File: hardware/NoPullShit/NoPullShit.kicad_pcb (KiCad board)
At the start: 2 copper layers, 52 parts, among them J1 USB Power, J2 Load cell, J3 Batt+, J4 Batt-, J5 ICSP, J6 UART, J7 Spk+, J8 Spk-, Q1 BC808, Q1 S8550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

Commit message: Initial routing backup
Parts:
- removed the Q1 at (72.5, 67.1)
- removed the Q1 at (33.5, 66.5)
- removed the Q2 at (82.2, 52.4)
- removed the Q2 at (37.9, 66.5)
- removed the Q3 at (80.9, 58.2)
- removed the Q3 at (42.4, 66.5)
- added H1: MountingHole_Pad, MountingHole:MountingHole_2.2mm_M2_Pad_Via, F.Cu at (28.4, 62.4)
- added H2: MountingHole_Pad, MountingHole:MountingHole_2.2mm_M2_Pad_Via, F.Cu at (62.4, 62.4)
- added H3: MountingHole_Pad, MountingHole:MountingHole_2.2mm_M2_Pad_Via, F.Cu at (28.4, 33.4)
- added H4: MountingHole_Pad, MountingHole:MountingHole_2.2mm_M2_Pad_Via, F.Cu at (62.4, 33.4)
- added Q1: BC808, Package_TO_SOT_SMD:SOT-23, F.Cu at (50.8, 55.0)
- added Q2: BC817, Package_TO_SOT_SMD:SOT-23, F.Cu at (55.6, 37.5)
- added Q3: BC808, Package_TO_SOT_SMD:SOT-23, F.Cu at (59.6, 37.5)
- C13, C14: footprint Capacitor_SMD:C_0603_1608Metric -> Capacitor_SMD:C_1206_3216Metric
- J2: footprint Connector_PinHeader_2.54mm:PinHeader_1x04_P2.54mm_Vertical -> Connector_PinHeader_2.00mm:PinHeader_1x04_P2.00mm_Vertical
- J3, J4, J7, J8: footprint Connector_PinHeader_1.00mm:PinHeader_1x01_P1.00mm_Vertical -> TestPoint:TestPoint_THTPad_1.0x1.0mm_Drill0.5mm
- moved R14 71.2 mm to (30.4, 38.4), turned to 180 degrees
- moved C8 58.8 mm to (40.2, 49.5), turned to 270 degrees
- moved R15 53.7 mm to (35.4, 41.3)
- moved C7 52.0 mm to (42.7, 48.9)
- moved C9 51.7 mm to (42.7, 36.2)
- moved C11 51.2 mm to (37.0, 35.5), turned to 90 degrees
- moved R17 51.1 mm to (45.9, 48.9)
- moved R13 48.1 mm to (38.3, 49.5), turned to 270 degrees
- moved R16 47.4 mm to (42.7, 50.8)
- moved R6 44.2 mm to (56.9, 56.7)
- moved C10 43.9 mm to (48.4, 35.5), turned to 90 degrees
- moved D1 41.9 mm to (26.2, 40.6), turned to 270 degrees
- moved R8 41.7 mm to (53.1, 47.2), turned to 90 degrees
- moved R7 41.2 mm to (55.7, 54.8)
- moved J8 40.4 mm to (63.4, 37.6)
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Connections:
- U3 pad 10: /N_BATT_CHRG -> /LED_A
- U3 pad 11: /N_BATT_STDBY -> Net-(U3-Pad11)
- U3 pad 2: /LED_A -> Net-(U3-Pad2)
- U3 pad 25: Net-(U3-Pad25) -> /N_BATT_STDBY
- U3 pad 26: Net-(U3-Pad26) -> /N_BATT_CHRG
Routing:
- net VCC: track 0.00 -> 57.1 mm
- net Net-(C3-Pad1): track 0.00 -> 32.2 mm
- net /N_BATT_CHRG: track 0.00 -> 21.5 mm
- net /N_BATT_STDBY: track 0.00 -> 18.8 mm
- net Net-(C8-Pad1): track 0.00 -> 18.4 mm
- net Net-(J5-Pad5): track 0.00 -> 15.9 mm, vias 0 -> 1
- net Net-(C5-Pad2): track 0.00 -> 15.4 mm
- net Net-(C1-Pad1): track 0.00 -> 14.6 mm
- net Net-(J5-Pad3): track 0.00 -> 13.0 mm
- net Net-(J1-Pad1): track 0.00 -> 12.2 mm
- net Net-(C10-Pad2): track 0.00 -> 12.1 mm
- net Net-(C13-Pad2): track 0.00 -> 10.7 mm
- net Net-(J2-Pad2): track 0.00 -> 9.37 mm
- net Net-(J2-Pad3): track 0.00 -> 9.28 mm
- net Net-(Q2-Pad1): track 0.00 -> 8.89 mm
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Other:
- board outline added: 40 x 35 mm
- board text added: "A+"
- board text added: "A-"
- board text added: "Batt+"
- board text added: "Batt-"
- board text added: "E+"
- board text added: "E-"
- board text added: "Sp+"
- board text added: "Sp-"

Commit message: Finished initla routing
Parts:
- moved R18 7.08 mm to (49.8, 35.5)
- moved C12 5.79 mm to (55.1, 39.5)
- moved C10 2.83 mm to (48.5, 32.7)
- moved Q3 2.51 mm to (57.8, 35.7)
- moved Q2 2.51 mm to (53.8, 35.7)
- moved C13 1.61 mm to (59.7, 41.8)
- moved C14 1.61 mm to (59.7, 39.2)
- moved J7 0.57 mm to (63.9, 42.9)
- moved J8 0.57 mm to (63.9, 37.8)
- moved R16 0.47 mm to (42.7, 51.2)
- moved C8 0.30 mm to (39.9, 49.5)
- moved C9 0.25 mm to (42.7, 35.9)
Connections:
- U3 pad 1: /RATE -> /DOUT
- U3 pad 14: /SCK -> Net-(U3-Pad14)
- U3 pad 2: Net-(U3-Pad2) -> /SCK
- U3 pad 32: /DOUT -> /RATE
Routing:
- net GND: track 0.00 -> 28.3 mm, vias 0 -> 24
- net /SCK: track 0.00 -> 23.2 mm
- net /DOUT: track 0.00 -> 20.4 mm
- net Net-(J5-Pad4): track 6.73 -> 23.4 mm, vias 0 -> 2
- net /RATE: track 0.00 -> 12.8 mm
- net /LED_A: track 0.00 -> 12.7 mm
- net /LED_B: track 0.00 -> 7.78 mm
- net Net-(D1-Pad1): track 0.00 -> 4.00 mm
- net VCC: track 57.1 -> 59.4 mm, vias 0 -> 4
- net Net-(J5-Pad5): track 15.9 -> 17.9 mm
- net Net-(Q2-Pad1): track 8.89 -> 7.34 mm
- net Net-(C13-Pad2): track 10.7 -> 11.8 mm
- added copper zone on B.Cu, net GND
- added copper zone on F.Cu, net GND

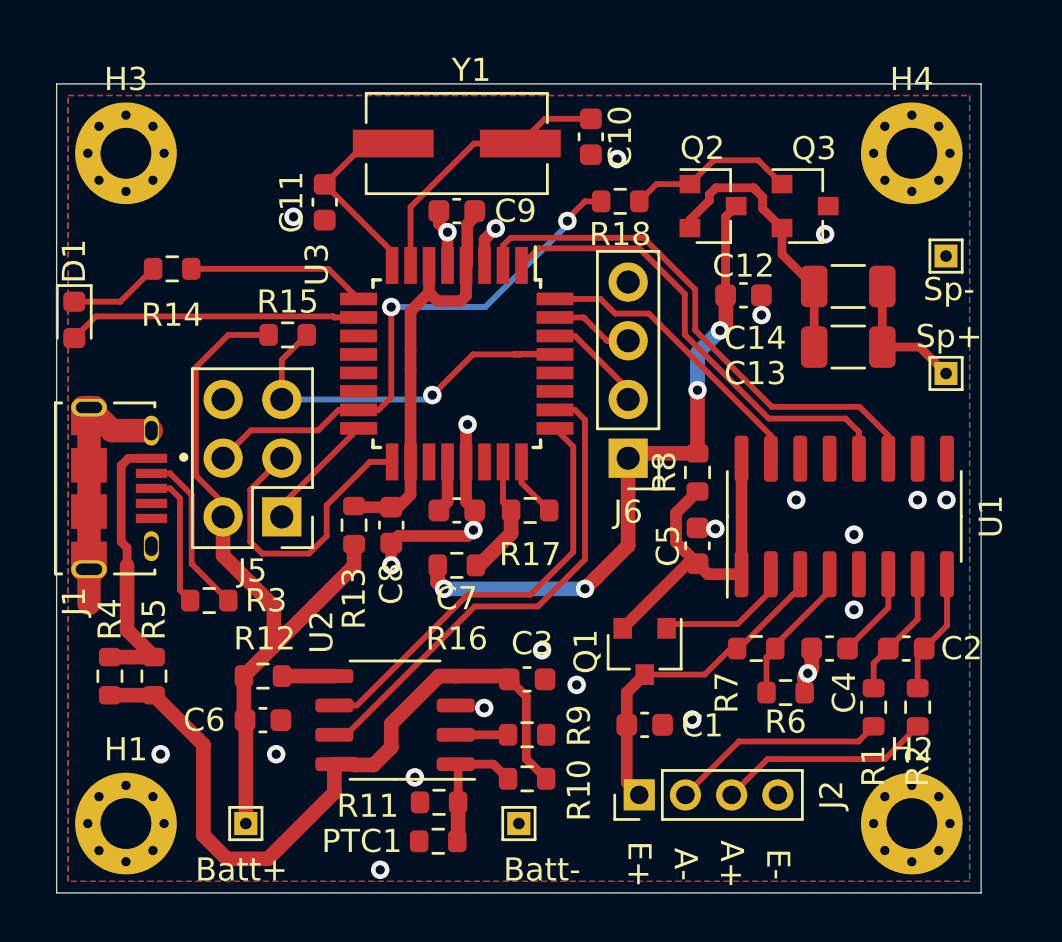
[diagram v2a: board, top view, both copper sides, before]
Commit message: Fixed RefDes placement
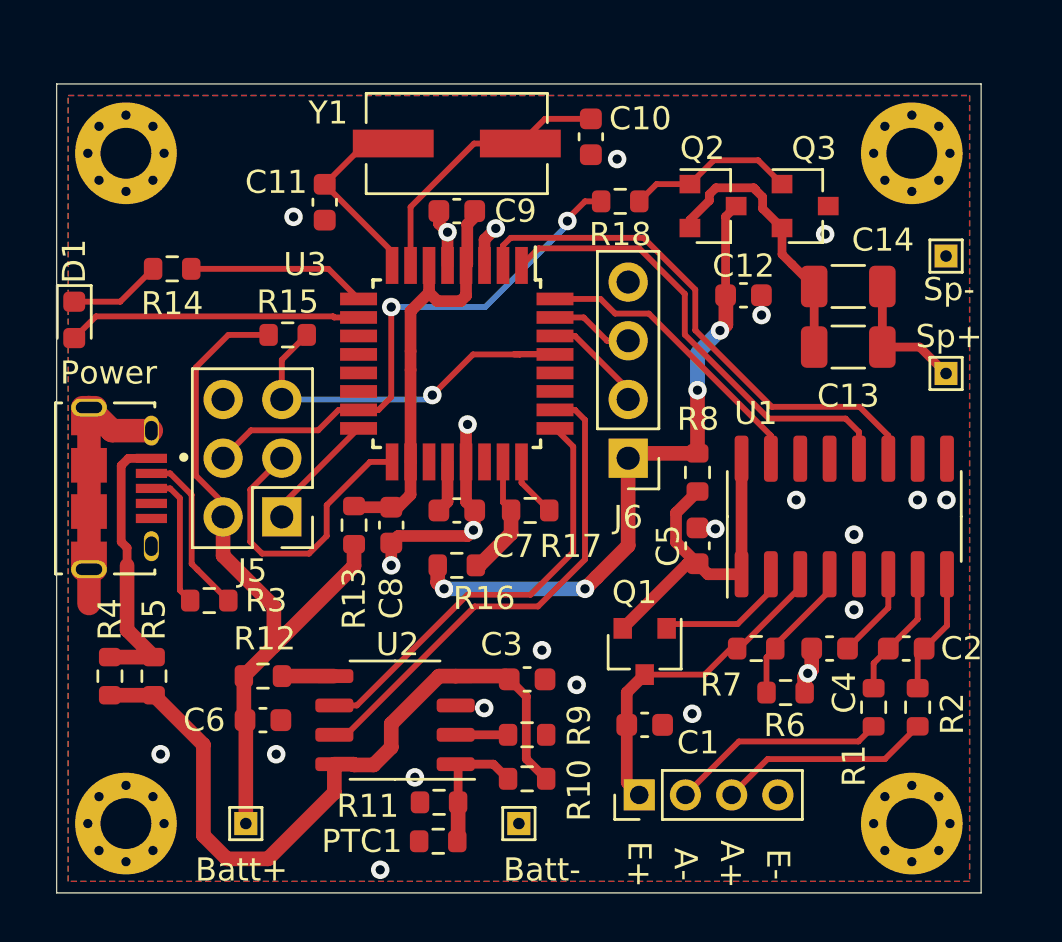
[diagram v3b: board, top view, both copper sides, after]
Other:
- board text added: "Power"

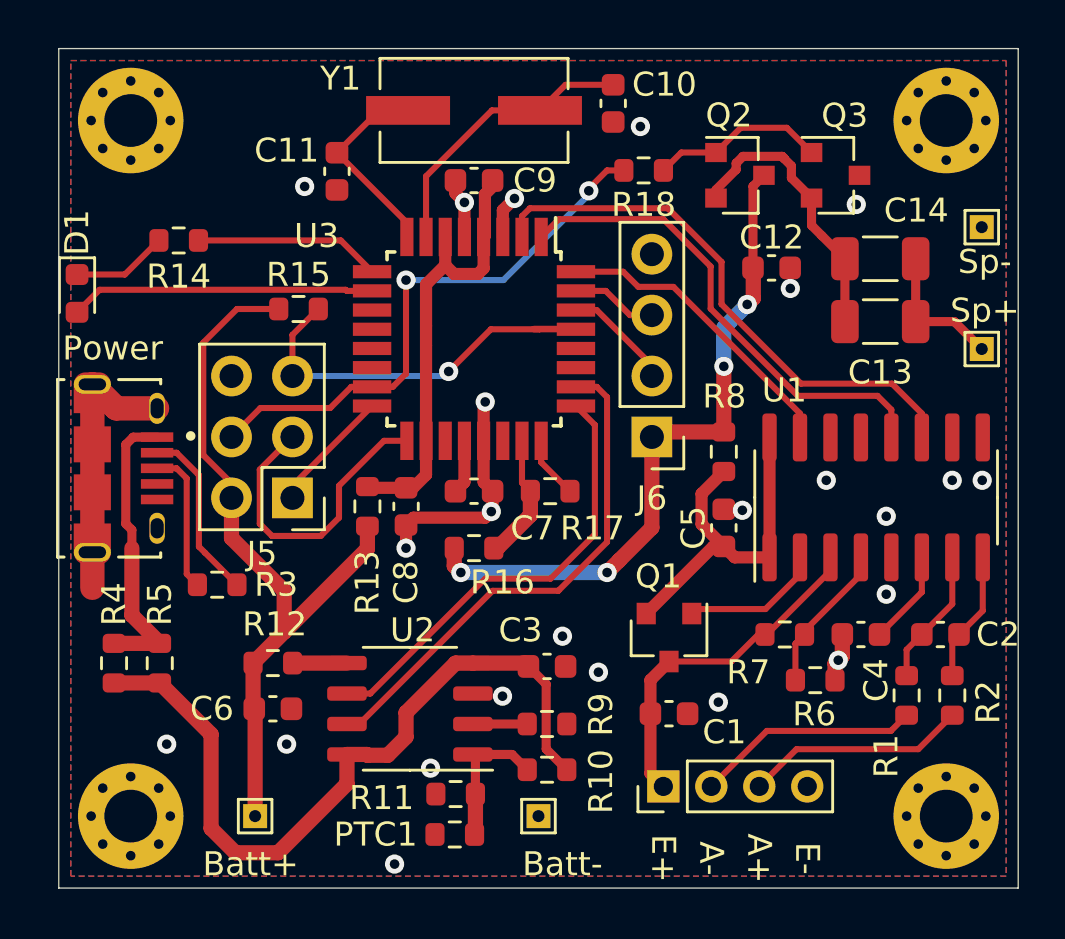
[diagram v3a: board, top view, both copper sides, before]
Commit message: Small layout changes
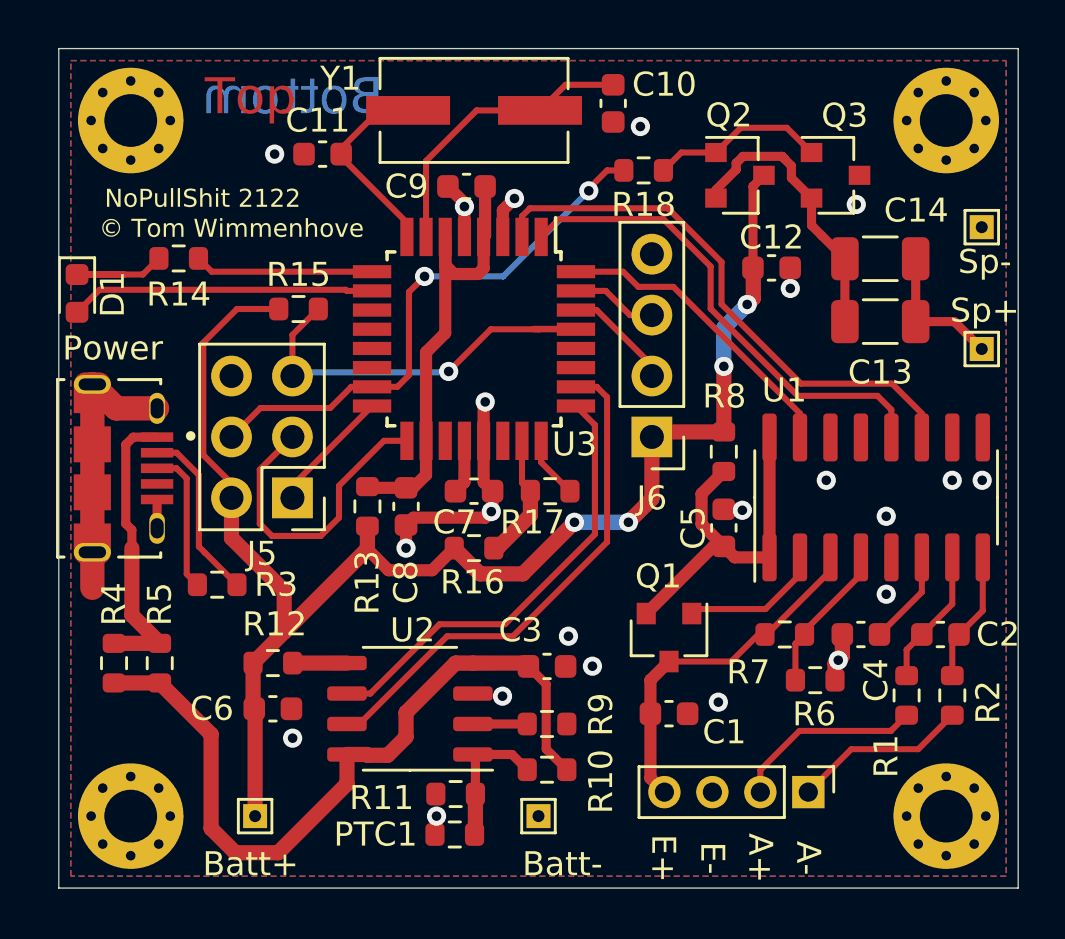
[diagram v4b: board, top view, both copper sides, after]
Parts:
- moved J2 6.05 mm to (56.6, 61.4), turned to 270 degrees
- moved C11 0.93 mm to (36.4, 34.8), turned to 0 degrees
- moved R14 0.75 mm to (30.4, 39.1)
- moved C9 0.40 mm to (42.4, 36.1)
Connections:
- J2 pad 1: Net-(C1-Pad1) -> Net-(J2-Pad1)
- J2 pad 3: Net-(J2-Pad3) -> GND
- J2 pad 4: GND -> Net-(C1-Pad1)
- R2 pad 2: Net-(J2-Pad3) -> Net-(J2-Pad1)
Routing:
- net Net-(J2-Pad3): track 9.28 -> 0.00 mm
- net Net-(J2-Pad1): track 0.00 -> 7.33 mm
- net VCC: track 59.4 -> 63.7 mm
- net Net-(D1-Pad1): track 4.00 -> 5.68 mm
- net Net-(J2-Pad2): track 9.37 -> 7.97 mm
- net GND: track 28.3 -> 29.5 mm, vias 24 -> 22
- net Net-(C8-Pad1): track 18.4 -> 19.4 mm
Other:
- board text added: "Bottom"
- board text added: "NoPullShit 2122"
- board text added: "Top"
- board text added: "© Tom Wimmenhove"

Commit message: Small small changes
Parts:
- C1, C3, C6: footprint Capacitor_SMD:C_0603_1608Metric -> Capacitor_SMD:C_0805_2012Metric
- J1: footprint Libraries:AMPHENOL_10118194-0001LF -> Connector_USB:USB_Micro-B_Amphenol_10103594-0001LF_Horizontal
- moved J1 1.45 mm to (28.2, 47.9)
- moved R3 0.76 mm to (32.0, 53.5)
- moved J5 0.42 mm to (35.6, 49.1)
- moved C6 0.42 mm to (34.3, 58.3)
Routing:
- net VCC: track 63.7 -> 65.8 mm
- net Net-(J5-Pad5): track 17.9 -> 16.7 mm
- net GND: track 29.5 -> 30.2 mm
- net Net-(J1-Pad3): track 6.02 -> 6.71 mm
- net Net-(J1-Pad2): track 7.36 -> 8.02 mm
- net Net-(J1-Pad1): track 12.2 -> 12.4 mm, vias 0 -> 2

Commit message: More smaller, more better
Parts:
- removed R13: 0R, Resistor_SMD:R_0603_1608Metric
- moved C10 19.3 mm to (29.7, 37.0), turned to 180 degrees
- moved J7 14.4 mm to (53.6, 32.8)
- moved Q2 12.7 mm to (41.4, 33.1)
- moved Q3 12.7 mm to (45.3, 33.1)
- moved R18 12.2 mm to (37.6, 34.4), turned to 270 degrees
- moved C13 11.9 mm to (49.7, 35.2)
- moved C14 11.9 mm to (49.7, 32.6)
- moved J8 10.4 mm to (53.6, 36.5)
- moved J6 10.1 mm to (57.6, 39.8), turned to 270 degrees
- moved C12 10.0 mm to (45.9, 35.6)
- moved Y1 9.42 mm to (33.8, 36.0), turned to 270 degrees
- moved C5 8.01 mm to (49.8, 43.1), turned to 180 degrees
- moved C11 7.78 mm to (29.7, 38.8), turned to 180 degrees
- moved H2 6.00 mm to (56.4, 62.4)
- moved C4 5.84 mm to (53.0, 54.8)
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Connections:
- C8 pad 1: Net-(C8-Pad1) -> VCC
- C9 pad 2: Net-(C8-Pad1) -> VCC
- U3 pad 18: Net-(C8-Pad1) -> VCC
- U3 pad 4: Net-(C8-Pad1) -> VCC
- U3 pad 6: Net-(C8-Pad1) -> VCC
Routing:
- net VCC: track 65.8 -> 97.7 mm, vias 4 -> 2
- net GND: track 30.2 -> 53.9 mm, vias 22 -> 26
- net Net-(C8-Pad1): track 19.4 -> 0.00 mm
- net /RATE: track 12.8 -> 26.3 mm
- net /N_BATT_CHRG: track 21.5 -> 28.1 mm
- net Net-(C10-Pad2): track 12.3 -> 17.8 mm
- net /N_BATT_STDBY: track 18.8 -> 24.2 mm
- net Net-(C3-Pad1): track 32.2 -> 27.1 mm, vias 0 -> 2
- net Net-(J5-Pad4): track 22.6 -> 18.0 mm
- net Net-(J6-Pad2): track 4.57 -> 9.14 mm
- net Net-(C11-Pad2): track 8.41 -> 12.2 mm
- net /DOUT: track 20.6 -> 23.7 mm
- net Net-(C5-Pad2): track 15.4 -> 18.4 mm
- net Net-(J6-Pad3): track 3.58 -> 6.55 mm
- net Net-(J1-Pad1): track 12.4 -> 9.53 mm
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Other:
- board size 40 x 35 mm -> 35 x 35 mm
- board text added: "B+"
- board text added: "B-"
- board text added: "S+"
- board text added: "S-"
- board text removed: "Batt+"
- board text removed: "Batt-"
- board text removed: "Power"
- board text removed: "Sp+"
- board text removed: "Sp-"

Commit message: Tiny optimizations
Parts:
- moved C11 0.22 mm to (29.9, 38.6), turned to 0 degrees
- moved C10 0.21 mm to (29.9, 36.9), turned to 0 degrees
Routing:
- net VCC: track 97.7 -> 104.1 mm
- net Net-(C11-Pad2): track 12.2 -> 9.48 mm
- net Net-(C10-Pad2): track 17.8 -> 15.7 mm
- net GND: track 53.9 -> 52.1 mm, vias 26 -> 22
- net Net-(J5-Pad4): track 18.0 -> 18.8 mm

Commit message: Neatify
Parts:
- moved R18 11.3 mm to (28.2, 40.6)
- moved C10 8.47 mm to (37.8, 34.0), turned to 180 degrees
- moved C11 8.38 mm to (37.8, 36.0), turned to 180 degrees
- moved Q2 3.98 mm to (45.3, 33.1)
- moved Q3 3.98 mm to (41.4, 33.1)
- moved R14 3.34 mm to (30.2, 37.3), turned to 90 degrees
- moved R15 2.05 mm to (30.2, 40.6), turned to 90 degrees
- moved R1 1.91 mm to (53.0, 57.2), turned to 180 degrees
- moved J4 1.55 mm to (41.3, 62.9)
- moved R6 1.35 mm to (49.8, 57.2)
- moved C3 1.09 mm to (40.8, 55.5)
- moved R10 1.09 mm to (40.8, 59.8)
- moved R9 1.09 mm to (40.8, 57.9)
- moved H2 1.00 mm to (57.4, 62.4)
- moved R11 0.81 mm to (37.0, 61.2)
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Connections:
- U3 pad 25: /N_BATT_STDBY -> /N_BATT_CHRG
- U3 pad 26: /N_BATT_CHRG -> /N_BATT_STDBY
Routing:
- net /N_BATT_STDBY: track 24.2 -> 41.2 mm
- net Net-(Q2-Pad1): track 7.91 -> 24.2 mm
- net /N_BATT_CHRG: track 28.1 -> 37.1 mm
- net VCC: track 104.1 -> 95.3 mm
- net Net-(C3-Pad1): track 27.1 -> 34.3 mm, vias 2 -> 0
- net Net-(C10-Pad2): track 15.7 -> 10.4 mm
- net /LED_A: track 12.8 -> 15.6 mm
- net Net-(D1-Pad1): track 3.04 -> 5.47 mm
- net Net-(J2-Pad2): track 7.97 -> 5.59 mm
- net Net-(C13-Pad2): track 14.2 -> 12.0 mm
- net /LED_B: track 8.49 -> 10.6 mm
- net Net-(J5-Pad5): track 19.4 -> 21.0 mm
- net GND: track 52.1 -> 53.6 mm, vias 22 -> 39
- net Net-(J5-Pad4): track 18.8 -> 17.6 mm, vias 2 -> 0
- net Net-(C2-Pad2): track 6.61 -> 7.71 mm
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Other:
- board text added: "2122"
- board text added: "NoPullShit"
- board text removed: "NoPullShit 2122"
